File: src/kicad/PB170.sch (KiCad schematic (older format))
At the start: 56 parts, among them J2 USB_B_Micro, Q1 BC817, Q2 BC817, Q3 BC817, Q4 BC817, SW1 SW_MEC_5E, U1 LM555xM, U10 74AUC1G74, U11 74AUC1G74, U13 74LS32, U14 74LS32, U15 74LS32, U16 74LS32, U17 74LS32, U18 74LS32, U19 74LS32, U20 74LS32, U21 74LS32, U5 74LS73, U6 74LS32, U7 74LS73, U8 74HC08, U9 74LVC2G32

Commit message: added sub-schemes
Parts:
- removed U14: 74LS32, symbol 74xx:74LS32
- added U?: 74LS32, symbol 74xx:74LS32
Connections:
- net labels added: D1!Q, D1Q, D2!Q, D2Q, JK1!Q, JK1Q, JK2!Q, JK2Q
- wire segments 112 -> 147
- no-connect marks 34 -> 12

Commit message: added OR gates
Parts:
- removed D11, D6, D8: LED white, LEDs:LED_0603, symbol Device:LED
- removed D13, D4, D7: LED green, LEDs:LED_0603, symbol Device:LED
- removed D3, D5, D9: LED blue, LEDs:LED_0603, symbol Device:LED
- removed R10, R7: 220R, Resistors_SMD:R_0603, symbol Device:R
- removed R13, R8, R9: 130R, Resistors_SMD:R_0603, symbol Device:R
- removed R15: 180R, Resistors_SMD:R_0603, symbol Device:R
- removed U13, U15, U16, U17, U18, U19, U20, U21, U6, U?: 74LS32, symbol 74xx:74LS32
- removed U9: 74LVC2G32, symbol 74xGxx:74LVC2G32
- added DB1, DB3: LED blue, LEDs:LED_0603, symbol Device:LED
- added DG1, DG2: LED green, LEDs:LED_0603, symbol Device:LED
- added DR2, DR3: LED red, LEDs:LED_0603, symbol Device:LED
- added DY1, DY2, DY3: LED yellow, LEDs:LED_0603, symbol Device:LED
- added O1, O2, O3: 74HC32, Housings_SOIC:SOIC-14_3.9x8.7mm_Pitch1.27mm, symbol PB170:74HC32
- added R?, RB1: 220R, Resistors_SMD:R_0603, symbol Device:R
- added RG1, RG2, RY1, RY2: 180R, Resistors_SMD:R_0603, symbol Device:R
- DR1: renamed from D1; value LED white -> LED red; LCSC C2290 -> C2286
- U1: value LM555xM -> 74HC08; footprint Package_SO:SOIC-8_3.9x4.9mm_P1.27mm -> Housings_SOIC:SOIC-14_3.9x8.7mm_Pitch1.27mm
- renumbered D12 to DB2, D10 to DG3, R14 to RB2, R12 to RG3, R6 to RY3, U8 to U1
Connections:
- wire segments 147 -> 173

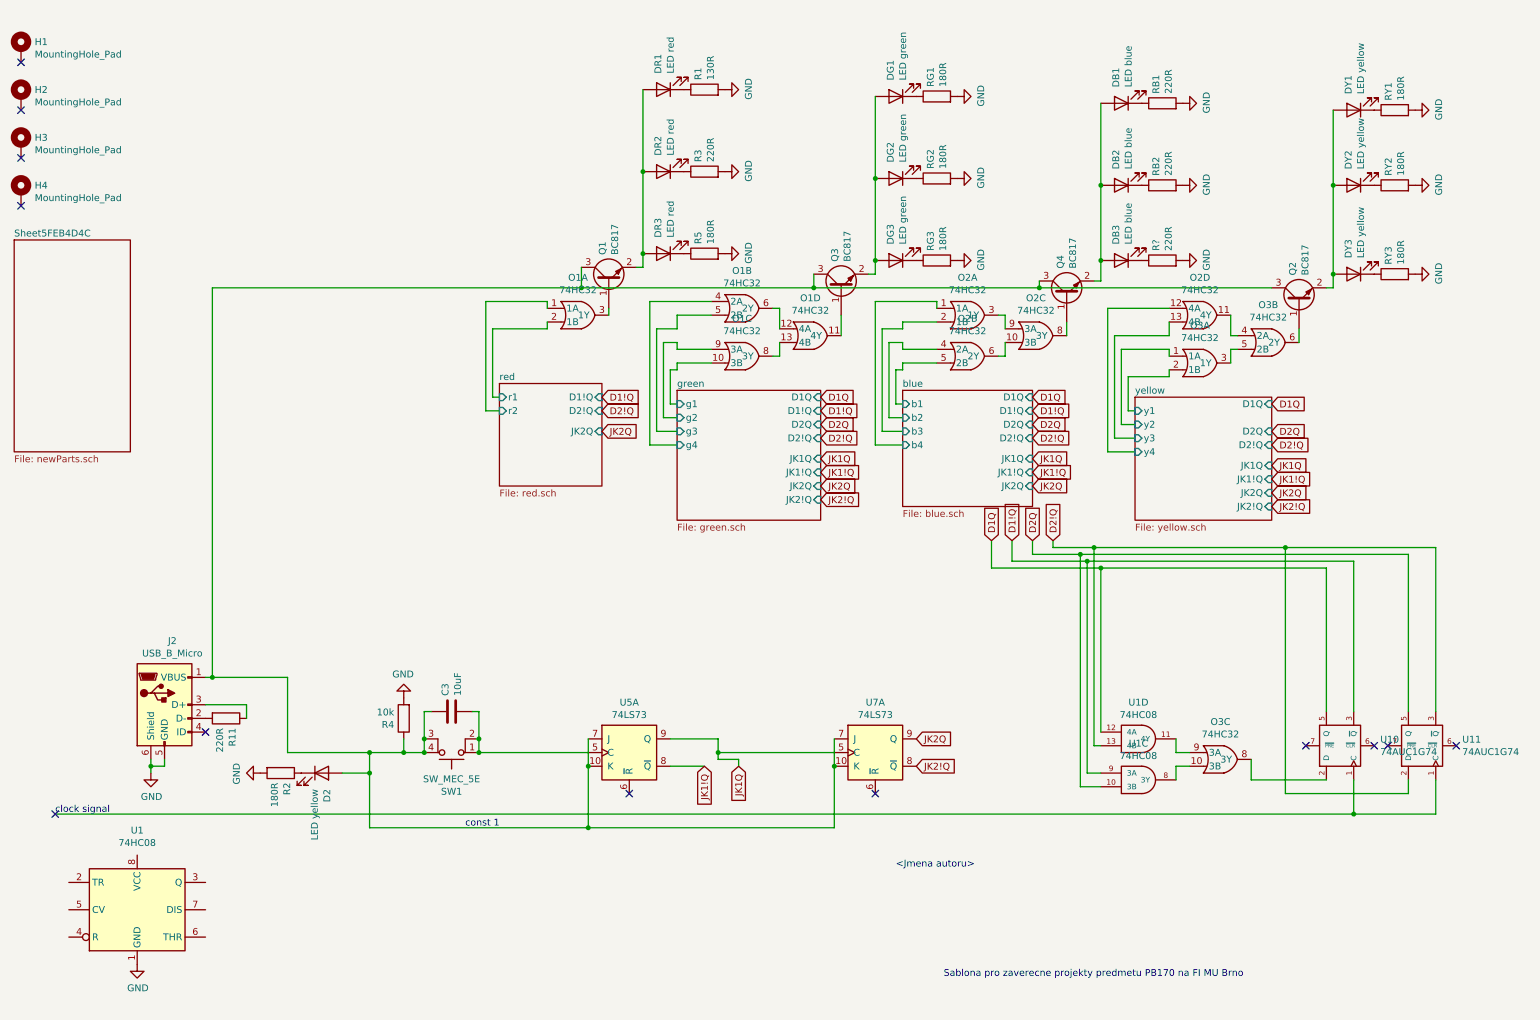
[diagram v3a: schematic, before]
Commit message: added D flip flops
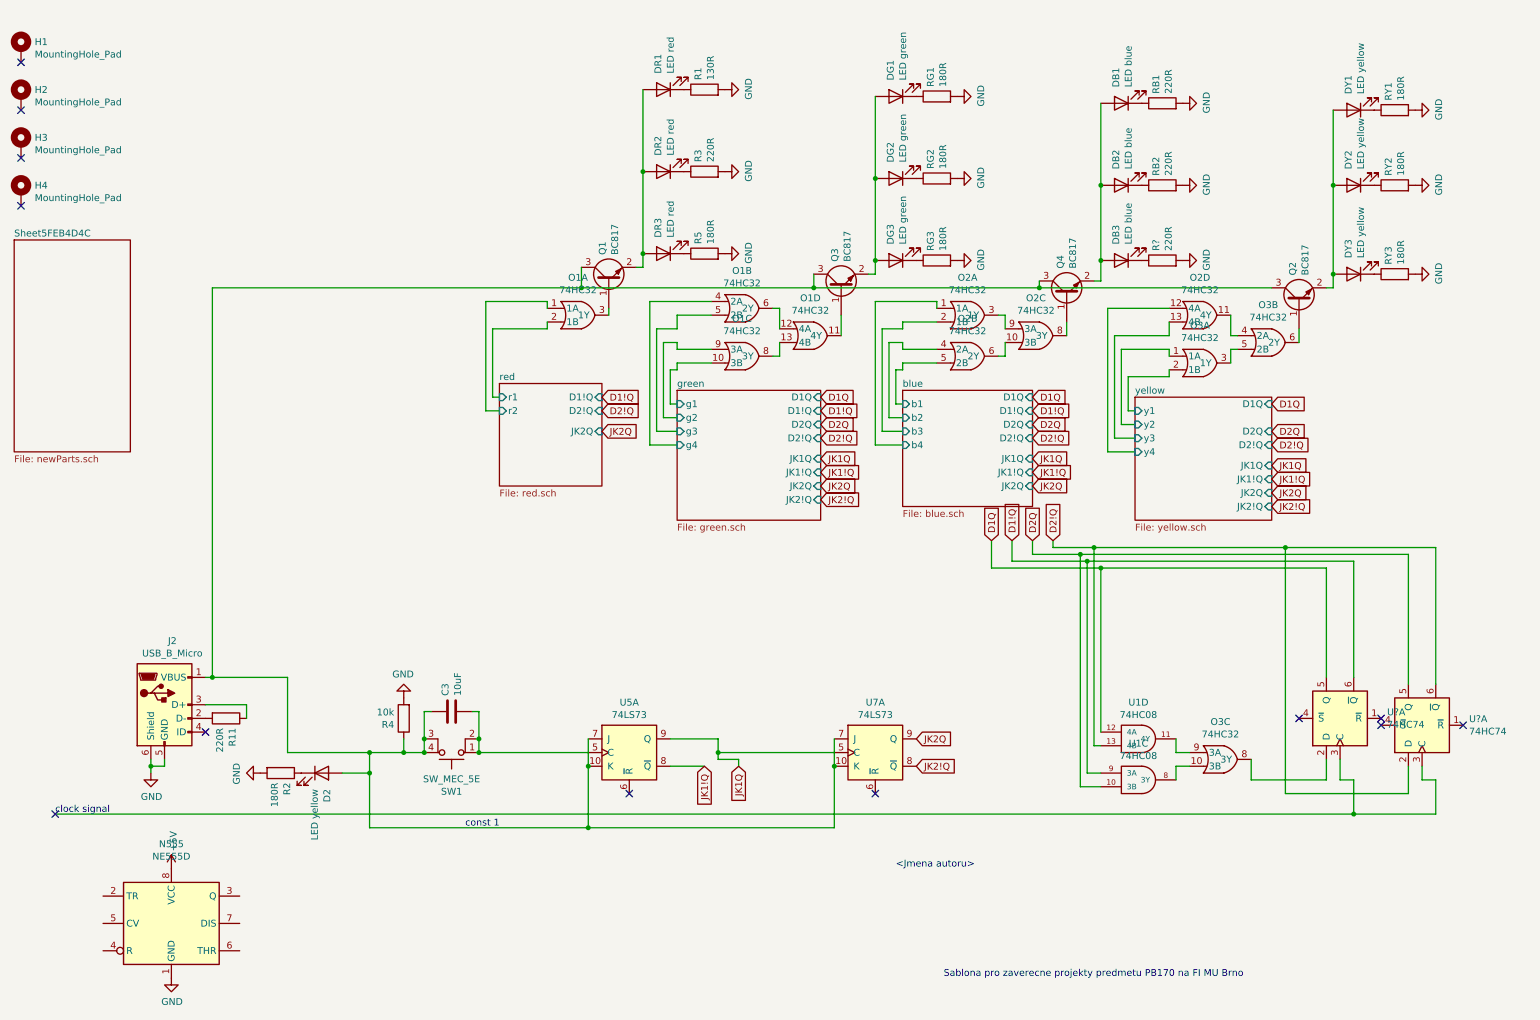
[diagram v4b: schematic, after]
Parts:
- removed unit 1 of U1
- removed U10, U11: 74AUC1G74, symbol 74xGxx:74AUC1G74
- added N555: NE555D, Package_SO:SOIC-8_3.9x4.9mm_P1.27mm, symbol Timer:NE555D
- added U? (x2): 74HC74, Housings_SSOP:TSSOP-14_4.4x5mm_Pitch0.65mm, symbol 74xx:74HC74
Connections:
- net D1!Q: now also U?.6 (~Q)
- net D1Q: now also U?.5 (Q)
- net D2!Q: now also U?.2 (D), U?.6 (~Q)
- net D2Q: now also U?.5 (Q)
- net GND: now also N555.1 (GND)
- net at O3.8 (3Y): now also U?.2 (D)
- new net: U?.3 (C), U?.3 (C)
- new net +5V: N555.8 (VCC)
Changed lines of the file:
@@
 	1    0    0    -1
 $EndComp
-$Comp
-L 74xGxx:74AUC1G74 U11
-U 1 1 60079BD5
-P 10900 5800
-F 0 "U11" V 10946 5506 50  0000 R CNN
-F 1 "74AUC1G74" V 10855 5506 50  0000 R CNN
-F 2 "" H 10900 5800 50  0001 C CNN
-F 3 "http://www.ti.com/lit/sg/scyt129e/scyt129e.pdf" H 10900 5800 50  0001 C CNN
-	1    10900 5800
-	0    -1   -1   0
-$EndComp
-$Comp
-L 74xGxx:74AUC1G74 U10
-U 1 1 6008142D
-P 10300 5800
-F 0 "U10" V 10346 5506 50  0000 R CNN
-F 1 "74AUC1G74" V 10255 5506 50  0000 R CNN
-F 2 "" H 10300 5800 50  0001 C CNN
-F 3 "http://www.ti.com/lit/sg/scyt129e/scyt129e.pdf" H 10300 5800 50  0001 C CNN
-	1    10300 5800
-	0    -1   -1   0
-$EndComp
-Wire Wire Line
-	10200 4500 10200 5550
 Wire Wire Line
 	10400 6050 10400 6300
@@
 	9650 6050 10200 6050
 Wire Wire Line
-	10400 5550 10400 4450
-Wire Wire Line
-	10800 5550 10800 4400
-Wire Wire Line
-	11000 5550 11000 4350
-Wire Wire Line
 	8550 5700 8550 4500
 Wire Wire Line
@@
 Wire Wire Line
 	8400 4400 10800 4400
-Wire Wire Line
-	10800 6050 10800 6150
 Wire Wire Line
 	10800 6150 9900 6150
@@
 Connection ~ 4800 6400
 NoConn ~ 900  6300
-NoConn ~ 10550 5800
-NoConn ~ 10650 5800
-NoConn ~ 10050 5800
-NoConn ~ 11150 5800
+NoConn ~ 10600 5600
+NoConn ~ 10000 5600
+NoConn ~ 11200 5650
 Wire Wire Line
 	4000 5850 4800 5850
@@
 Wire Wire Line
 	2050 2450 2050 5300
-$Comp
-L Timer:LM555xM U1
-U 1 1 5FFCEE1C
-P 1500 7000
-F 0 "U1" H 1500 7581 50  0000 C CNN
-F 1 "74HC08" H 1500 7490 50  0000 C CNN
-F 2 "Housings_SOIC:SOIC-14_3.9x8.7mm_Pitch1.27mm" H 2350 6600 50  0001 C CNN
-F 3 "https://datasheet.lcsc.com/szlcsc/Nexperia-74HC08D-653_C5593.pdf" H 2350 6600 50  0001 C CNN
-	1    1500 7000
-	1    0    0    -1
-$EndComp
 Wire Wire Line
 	6450 2350 6450 2450
@@
 Wire Wire Line
 	9200 5850 9100 5850
-$Comp
-L power:GND #PWR?
-U 1 1 6035291F
-P 1500 7400
-F 0 "#PWR?" H 1500 7150 50  0001 C CNN
-F 1 "GND" H 1505 7227 50  0000 C CNN
-F 2 "" H 1500 7400 50  0001 C CNN
-F 3 "" H 1500 7400 50  0001 C CNN
-	1    1500 7400
-	1    0    0    -1
-$EndComp
 Wire Wire Line
 	5200 1000 5200 1600
@@
 Wire Wire Line
 	5200 1600 5200 2200
+$Comp
+L Timer:NE555D N555
+U 1 1 601C8779
+P 1750 7100
+F 0 "N555" H 1750 7681 50  0000 C CNN
+F 1 "NE555D" H 1750 7590 50  0000 C CNN
+F 2 "Package_SO:SOIC-8_3.9x4.9mm_P1.27mm" H 2600 6700 50  0001 C CNN
+F 3 "https://datasheet.lcsc.com/szlcsc/Texas-Instruments-TI-NE555DR_C7593.pdf" H 2600 6700 50  0001 C CNN
+F 4 "C7593" H 1750 7100 50  0001 C CNN "LCSC"
+	1    1750 7100
+	1    0    0    -1
+$EndComp
+$Comp
+L power:+5V #PWR?
+U 1 1 601DEE3F
+P 1750 6700
+AR Path="/601DEE3F" Ref="#PWR?"  Part="1"
+AR Path="/5FEB4D4D/601DEE3F" Ref="#PWR?"  Part="1"
+F 0 "#PWR?" H 1750 6550 50  0001 C CNN
+F 1 "+5V" V 1765 6828 50  0000 L CNN
+F 2 "" H 1750 6700 50  0001 C CNN
+F 3 "" H 1750 6700 50  0001 C CNN
+	1    1750 6700
+	1    0    0    -1
+$EndComp
+$Comp
+L power:GND #PWR?
+U 1 1 601E7CDC
+P 1750 7500
+F 0 "#PWR?" H 1750 7250 50  0001 C CNN
+F 1 "GND" H 1755 7327 50  0000 C CNN
+F 2 "" H 1750 7500 50  0001 C CNN
+F 3 "" H 1750 7500 50  0001 C CNN
+	1    1750 7500
+	1    0    0    -1
+$EndComp
+Wire Wire Line
+	10300 6050 10400 6050
+Wire Wire Line
+	11000 6050 10900 6050
+Wire Wire Line
+	11000 4350 11000 5350
+Wire Wire Line
+	10800 4400 10800 5350
+Wire Wire Line
+	10400 4450 10400 5300
+Wire Wire Line
+	10200 4500 10200 5300
+Wire Wire Line
+	10900 6050 10900 5950
+Wire Wire Line
+	10800 5950 10800 6150
+Wire Wire Line
+	10300 5900 10300 6050
+Wire Wire Line
+	10200 5900 10200 6050
+NoConn ~ 10600 5650
+$Comp
+L 74xx:74HC74 U?
+U 1 1 601F0AD7
+P 10900 5650
+F 0 "U?" V 10946 5306 50  0000 R CNN
+F 1 "74HC74" V 10855 5306 50  0000 R CNN
+F 2 "Housings_SSOP:TSSOP-14_4.4x5mm_Pitch0.65mm" H 10900 5650 50  0001 C CNN
+F 3 "74xx/74hc_hct74.pdf" H 10900 5650 50  0001 C CNN
+	1    10900 5650
+	0    -1   -1   0
+$EndComp
+$Comp
+L 74xx:74HC74 U?
+U 1 1 601F3650
+P 10300 5600
+F 0 "U?" V 10346 5256 50  0000 R CNN
+F 1 "74HC74" V 10255 5256 50  0000 R CNN
+F 2 "Housings_SSOP:TSSOP-14_4.4x5mm_Pitch0.65mm" H 10300 5600 50  0001 C CNN
+F 3 "74xx/74hc_hct74.pdf" H 10300 5600 50  0001 C CNN
+	1    10300 5600
+	0    -1   -1   0
+$EndComp
 $EndSCHEMATC

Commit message: D flops edit
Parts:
- gave numbers to parts that had none: 1
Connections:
- net D2!Q: now also D1.12 (D), D1.8 (~Q); no longer D1.2 (D), D1.6 (~Q)
- net D2Q: now also D1.9 (Q); no longer D1.5 (Q)
- net at D1.3 (C): now also D1.11 (C); no longer D1.3 (C)
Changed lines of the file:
@@
 NoConn ~ 10600 5650
 $Comp
-L 74xx:74HC74 U?
-U 1 1 601F0AD7
+L 74xx:74HC74 D1
+U 2 1 601F0AD7
 P 10900 5650
-F 0 "U?" V 10946 5306 50  0000 R CNN
+F 0 "D1" V 10946 5306 50  0000 R CNN
 F 1 "74HC74" V 10855 5306 50  0000 R CNN
 F 2 "Housings_SSOP:TSSOP-14_4.4x5mm_Pitch0.65mm" H 10900 5650 50  0001 C CNN
 F 3 "74xx/74hc_hct74.pdf" H 10900 5650 50  0001 C CNN
-	1    10900 5650
+	2    10900 5650
 	0    -1   -1   0
 $EndComp
 $Comp
-L 74xx:74HC74 U?
+L 74xx:74HC74 D1
 U 1 1 601F3650
 P 10300 5600
-F 0 "U?" V 10346 5256 50  0000 R CNN
+F 0 "D1" V 10346 5256 50  0000 R CNN
 F 1 "74HC74" V 10255 5256 50  0000 R CNN
 F 2 "Housings_SSOP:TSSOP-14_4.4x5mm_Pitch0.65mm" H 10300 5600 50  0001 C CNN

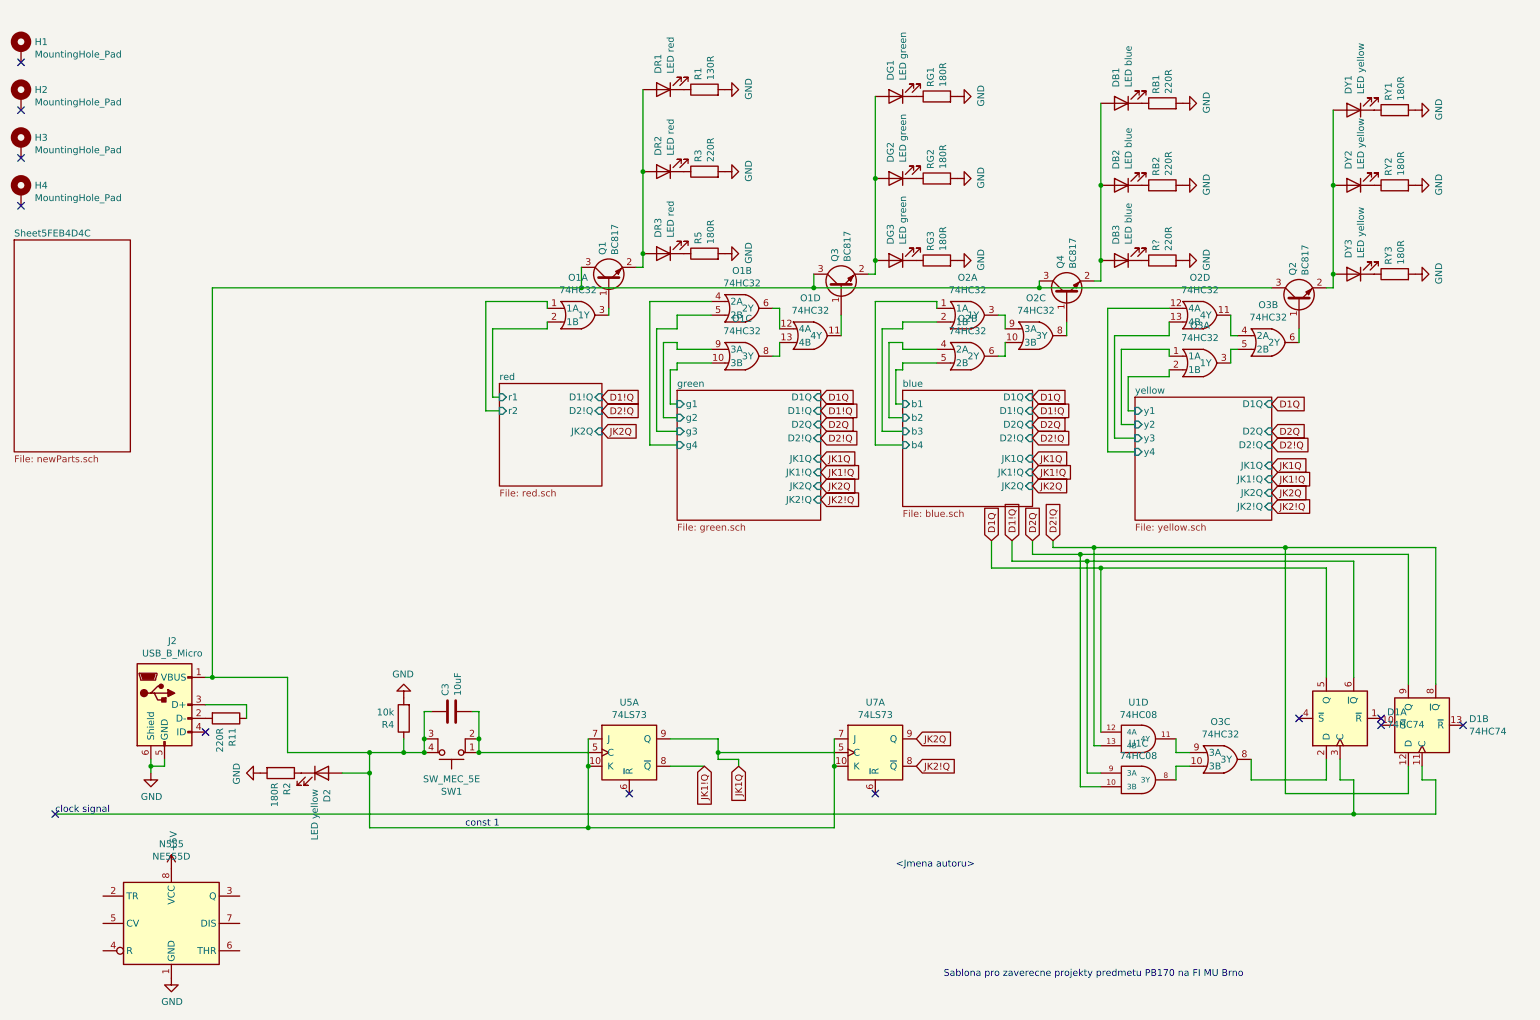
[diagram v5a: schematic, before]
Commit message: 555 clk implementation
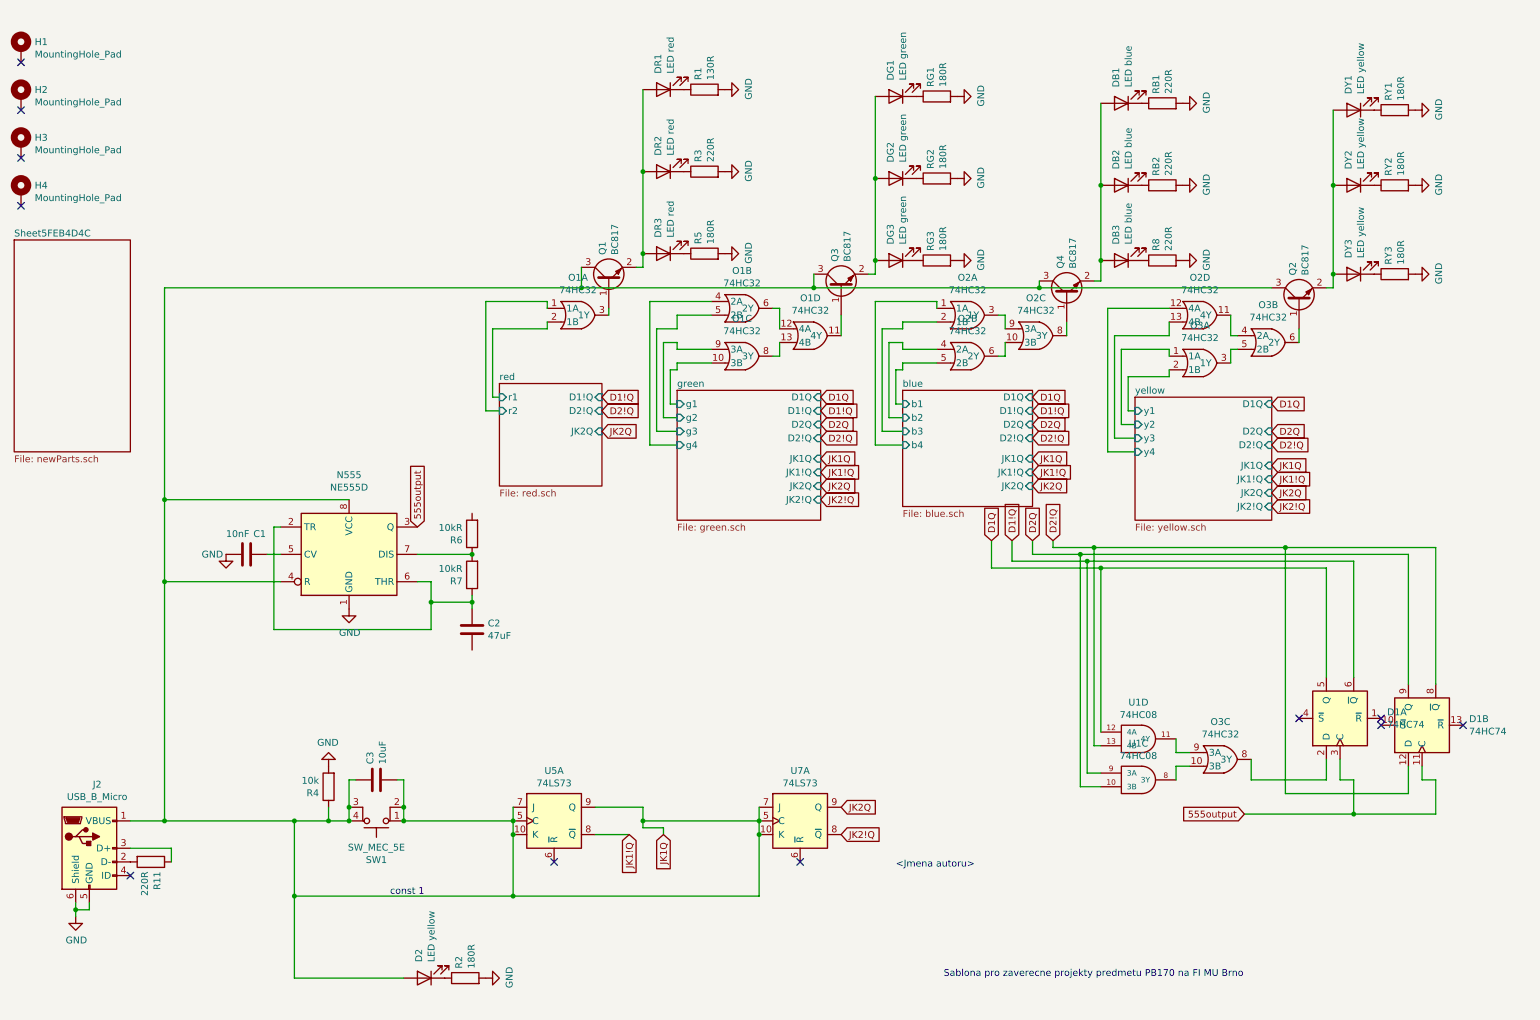
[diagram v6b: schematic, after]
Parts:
- added C1: 10nF, Capacitors_SMD:C_0805, symbol Device:C
- added C2: 47uF, Capacitors_SMD:C_1206, symbol Device:C
- added R6, R7: 10kR, Resistors_SMD:R_0603, symbol Device:R
- gave numbers to parts that had none: 1
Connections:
- net +5V is gone; now on net JK1Q: N555.8 (VCC)
- net GND: now also C1.2
- net JK1Q: now also C3.1, C3.2, D2.2 (A), J2.1 (VBUS), N555.4 (R), Q1.3 (C), Q2.3 (C), Q3.3 (C), Q4.3 (C), R4.1, SW1.1, SW1.2, SW1.3 (K), SW1.4 (A), U5.10 (K), U5.5 (C), U5.7 (J), U7.10 (K), U7.7 (J)
- net at N555.2 (TR): now also N555.6 (THR), C2.1, R7.1
- net 555output: now reaches N555.3 (Q)
- net 555output: now also D1.11 (C), D1.3 (C)
- net at N555.5 (CV): now also C1.1
- net at N555.7 (DIS): now also R6.1, R7.2
- no-connect marks 12 -> 11
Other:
- note removed: "clock signal"
- moved on the sheet: C3, D2, J2, N555, R11, R2, R4, SW1, U5A, U7A

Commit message: fixed annotaion
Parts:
- renumbered U5 to U20, U7 to U21
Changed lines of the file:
@@
 $Descr A4 11693 8268
 encoding utf-8
-Sheet 1 6
+Sheet 1 5
 Title ""
 Date ""
@@
 NoConn ~ 650  1500
 NoConn ~ 650  1850
-$Sheet
-S 600  2100 850  1550
-U 5FEB4D4D
-F0 "Sheet5FEB4D4C" 50
-F1 "newParts.sch" 50
-$EndSheet
 $Comp
 L Device:LED DB2
@@
 $EndComp
 $Comp
-L 74xx:74LS73 U5
+L 74xx:74LS73 U20
 U 1 1 5FFFB942
 P 4550 6350
-F 0 "U5" H 4550 6717 50  0000 C CNN
+F 0 "U20" H 4550 6717 50  0000 C CNN
 F 1 "74LS73" H 4550 6626 50  0000 C CNN
 F 2 "" H 4550 6350 50  0001 C CNN
@@
 $EndComp
 $Comp
-L 74xx:74LS73 U7
+L 74xx:74LS73 U21
 U 1 1 6000B5B4
 P 6350 6350
-F 0 "U7" H 6350 6717 50  0000 C CNN
+F 0 "U21" H 6350 6717 50  0000 C CNN
 F 1 "74LS73" H 6350 6626 50  0000 C CNN
 F 2 "" H 6350 6350 50  0001 C CNN
